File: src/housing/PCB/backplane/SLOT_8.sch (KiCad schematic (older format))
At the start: 1 part, among them J7 10018784-10201TLF

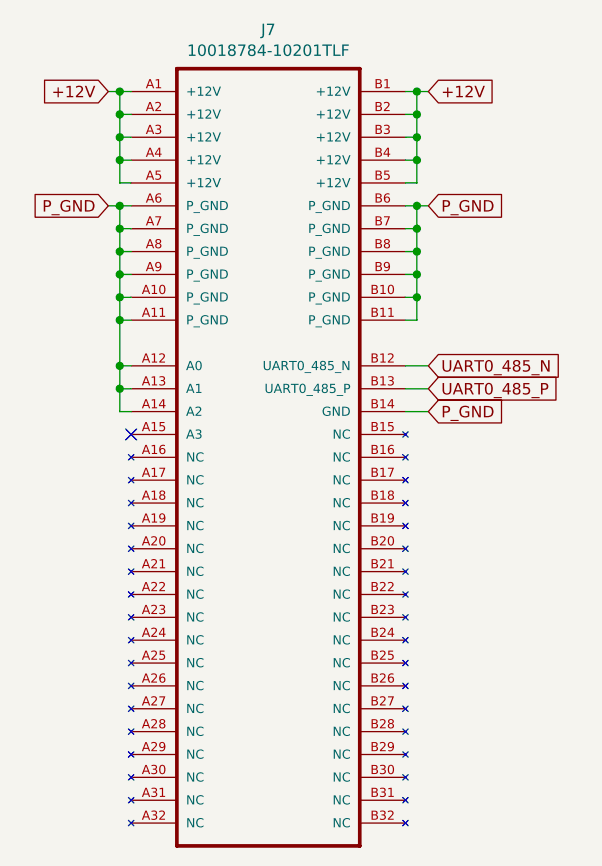
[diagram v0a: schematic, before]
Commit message: fixing backplane libraries path error
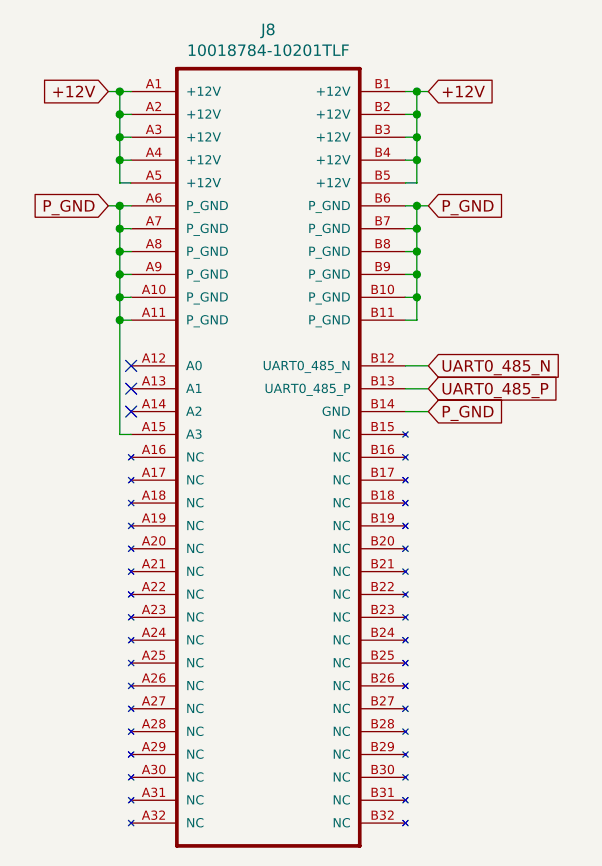
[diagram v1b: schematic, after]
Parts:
- removed J7: 10018784-10201TLF, kicad-lib:CONN_10018784-10201TLF, symbol 10018784-10201TLF:10018784-10201TLF
- added J8: 10018784-10201TLF, kicad-lib:CONN_10018784-10201TLF, symbol 10018784-10201TLF:10018784-10201TLF
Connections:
- net +12V: now also J8.A1 (+12V), J8.A2 (+12V), J8.A3 (+12V), J8.A4 (+12V), J8.A5 (+12V), J8.B1 (+12V), J8.B2 (+12V), J8.B3 (+12V), J8.B4 (+12V), J8.B5 (+12V)
- net P_GND: now also J8.A10 (P_GND), J8.A11 (P_GND), J8.A15 (A3), J8.A6 (P_GND), J8.A7 (P_GND), J8.A8 (P_GND), J8.A9 (P_GND), J8.B10 (P_GND), J8.B11 (P_GND), J8.B14 (GND), J8.B6 (P_GND), J8.B7 (P_GND), J8.B8 (P_GND), J8.B9 (P_GND)
- net UART0_485_N: now also J8.B12 (UART0_485_N)
- net UART0_485_P: now also J8.B13 (UART0_485_P)
- no-connect marks 1 -> 3
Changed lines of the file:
@@
 $Descr A4 11693 8268
 encoding utf-8
-Sheet 8 9
-Title ""
+Sheet 9 9
+Title "ACS backplane"
 Date ""
-Rev ""
-Comp ""
-Comment1 ""
+Rev "1"
+Comp "Halidelabs"
+Comment1 "contact@halidelabs.eu"
 Comment2 ""
 Comment3 ""
@@
 $Comp
 L 10018784-10201TLF:10018784-10201TLF J?
-U 1 1 5DF52F0B
+U 1 1 5DF52F0A
 P 5600 3950
-AR Path="/5DF19C0C/5DF52F0B" Ref="J?"  Part="1"
-AR Path="/5DF2A71E/5DF52F0B" Ref="J?"  Part="1"
-AR Path="/5DF2E10A/5DF52F0B" Ref="J?"  Part="1"
-AR Path="/5DF2E1F6/5DF52F0B" Ref="J?"  Part="1"
-AR Path="/5DF2E246/5DF52F0B" Ref="J?"  Part="1"
-AR Path="/5DF2E24A/5DF52F0B" Ref="J7"  Part="1"
-F 0 "J7" H 5600 5820 50  0000 C CNN
+AR Path="/5DF19C0C/5DF52F0A" Ref="J?"  Part="1"
+AR Path="/5DF2A71E/5DF52F0A" Ref="J?"  Part="1"
+AR Path="/5DF2E10A/5DF52F0A" Ref="J?"  Part="1"
+AR Path="/5DF2E1F8/5DF52F0A" Ref="J?"  Part="1"
+AR Path="/5DF2E248/5DF52F0A" Ref="J?"  Part="1"
+AR Path="/5DF2E24C/5DF52F0A" Ref="J8"  Part="1"
+F 0 "J8" H 5600 5820 50  0000 C CNN
 F 1 "10018784-10201TLF" H 5600 5729 50  0000 C CNN
 F 2 "kicad-lib:CONN_10018784-10201TLF" H 5650 4450 50  0001 L BNN
@@
 Wire Wire Line
 	6300 3750 6200 3750
-Wire Wire Line
-	4950 3350 4950 3550
-Wire Wire Line
-	4950 3550 5000 3550
 Connection ~ 4950 3350
 Wire Wire Line
-	4950 3550 4950 3650
+	4950 3850 5000 3850
 Wire Wire Line
-	4950 3650 5000 3650
-Connection ~ 4950 3550
-Wire Wire Line
-	4950 3650 4950 3750
-Wire Wire Line
-	4950 3750 5000 3750
-Connection ~ 4950 3650
-NoConn ~ 5000 3850
+	4950 3350 4950 3850
+NoConn ~ 5000 3550
+NoConn ~ 5000 3650
+NoConn ~ 5000 3750
 $EndSCHEMATC
